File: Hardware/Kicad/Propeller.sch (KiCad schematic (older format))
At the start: 7 parts, among them IC201 P8X32A, IC202 24LC512, X201 5MHz

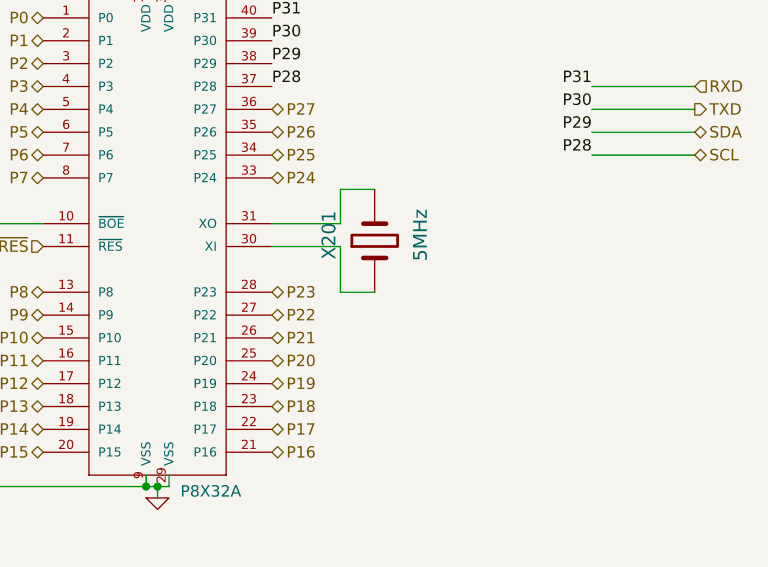
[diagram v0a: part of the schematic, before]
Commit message: Schematic updates
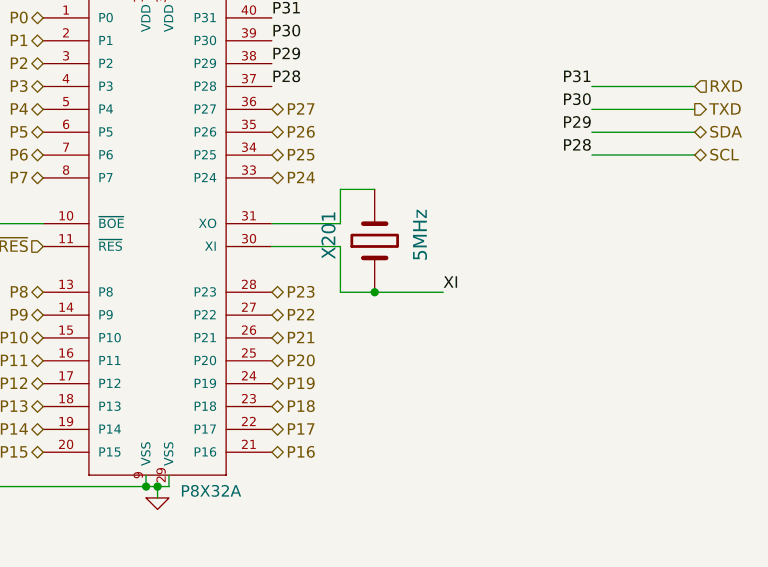
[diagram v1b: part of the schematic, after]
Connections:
- net XI: now reaches IC201.30 (XI), X201.1
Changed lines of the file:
@@
 Sheet 2 7
 Title "Propeddle"
-Date "8 apr 2014"
+Date "18 apr 2014"
 Rev "10"
 Comp "(C) 2014 Jac Goudsmit"
@@
 	6700 2600 6700 2800
 Wire Wire Line
-	6700 2800 6850 2800
+	6700 2800 7150 2800
 Text HLabel 5400 1600 0    50   BiDi ~ 0
 P0
@@
 	1    0    0    -1
 $EndComp
+Connection ~ 6850 2800
+Text Label 7150 2800 0    50   ~ 0
+XI
 $EndSCHEMATC
